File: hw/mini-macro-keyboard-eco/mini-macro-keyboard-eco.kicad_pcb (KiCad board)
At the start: 2 copper layers, 0 parts

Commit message: feat(hw): load netlist
Signed-off-by: Ivan Kovalenko <s1ckretbox@gmail.com>
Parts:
- added C0: 100n, Capacitor_SMD:C_0402_1005Metric, F.Cu at (64.6, 43.6)
- added C1: 100n, Capacitor_SMD:C_0402_1005Metric, F.Cu at (64.6, 45.6)
- added C10: 1u, Capacitor_SMD:C_0402_1005Metric, F.Cu at (79.3, 29.8)
- added C11: 1u, Capacitor_SMD:C_0402_1005Metric, F.Cu at (69.3, 41.1)
- added C2: 100n, Capacitor_SMD:C_0402_1005Metric, F.Cu at (82.2, 29.8)
- added C3: 100n, Capacitor_SMD:C_0402_1005Metric, F.Cu at (57.6, 53.7)
- added C4: 100n, Capacitor_SMD:C_0402_1005Metric, F.Cu at (63.5, 47.9)
- added C5: 100n, Capacitor_SMD:C_0402_1005Metric, F.Cu at (67.4, 43.0)
- added C6: 100n, Capacitor_SMD:C_0402_1005Metric, F.Cu at (79.3, 31.8)
- added C7: 4.7u, Capacitor_SMD:C_0402_1005Metric, F.Cu at (73.4, 38.5)
- added C8: 12p, Capacitor_SMD:C_0402_1005Metric, F.Cu at (60.6, 49.9)
- added C9: 12p, Capacitor_SMD:C_0402_1005Metric, F.Cu at (82.2, 27.8)
- added D1: BLUE, LED_SMD:LED_0603_1608Metric, F.Cu at (63.0, 38.8)
- added D2: BLUE, LED_SMD:LED_0603_1608Metric, F.Cu at (67.0, 38.8)
- added D3: BLUE, LED_SMD:LED_0603_1608Metric, F.Cu at (63.0, 41.4)
- added J0: USB_B_Micro, Connector_USB:USB_Micro-B_Molex-105017-0001, F.Cu at (46.2, 40.5)
- added J1: SWD, Connector_PinHeader_2.54mm:PinHeader_1x04_P2.54mm_Horizontal, F.Cu at (19.6, 39.8)
- added R0: 10k, Resistor_SMD:R_0402_1005Metric, F.Cu at (28.8, 50.7)
- added R1: 10k, Resistor_SMD:R_0402_1005Metric, F.Cu at (28.8, 52.7)
- added R11: 330, Resistor_SMD:R_0603_1608Metric, F.Cu at (61.1, 45.6)
- added R12: 330, Resistor_SMD:R_0603_1608Metric, F.Cu at (79.9, 25.6)
- added R13: 330, Resistor_SMD:R_0603_1608Metric, F.Cu at (79.9, 23.1)
- added R2: 10k, Resistor_SMD:R_0402_1005Metric, F.Cu at (60.6, 47.9)
- added R3: 10k, Resistor_SMD:R_0402_1005Metric, F.Cu at (51.8, 53.7)
- added R4: 10k, Resistor_SMD:R_0402_1005Metric, F.Cu at (66.4, 41.1)
- added R5: 10k, Resistor_SMD:R_0402_1005Metric, F.Cu at (79.3, 27.8)
- added R6: 10k, Resistor_SMD:R_0402_1005Metric, F.Cu at (70.5, 38.5)
- added R7: 47, Resistor_SMD:R_0402_1005Metric, F.Cu at (54.7, 53.7)
- added SW0: SW_SPDT, Button_Switch_SMD:SW_SPDT_PCM12, F.Cu at (45.5, 49.0)
- added SW1: SW_1, Button_Switch_Keyboard:SW_Cherry_MX_1.00u_PCB, F.Cu at (29.9, 22.3)
- added SW2: SW_2, Button_Switch_Keyboard:SW_Cherry_MX_1.00u_PCB, F.Cu at (50.1, 22.3)
- added SW3: SW_3, Button_Switch_Keyboard:SW_Cherry_MX_1.00u_PCB, F.Cu at (70.3, 22.3)
- added SW4: RESET, Button_Switch_THT:SW_PUSH_6mm, F.Cu at (32.7, 39.5)
- added SW5: SW_SPDT, Button_Switch_SMD:SW_SPDT_PCM12, F.Cu at (56.0, 40.5)
- added SW6: SW_SPDT, Button_Switch_SMD:SW_SPDT_PCM12, F.Cu at (35.6, 49.0)
- added U1: USBLC6-2SC6, Package_TO_SOT_SMD:SOT-23-6, F.Cu at (25.0, 52.1)
- added U2: XC6206P322MR, Package_TO_SOT_SMD:SOT-23, F.Cu at (80.1, 19.6)
- added U3: STM32F070F6Px, Package_SO:TSSOP-20_4.4x6.5mm_P0.65mm, F.Cu at (54.8, 48.7)
- added Y1: 16 MHz, Crystal:Crystal_SMD_3225-4Pin_3.2x2.5mm, F.Cu at (19.9, 52.0)

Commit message: feat(hw): add rough layout
Signed-off-by: Ivan Kovalenko <s1ckretbox@gmail.com>
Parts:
- moved J1 151.3 mm to (162.7, 89.0), turned to 90 degrees
- moved SW6 131.9 mm to (163.3, 81.9), turned to 180 degrees
- moved SW4 124.4 mm to (149.2, 83.1)
- moved R13 121.8 mm to (167.1, 108.2)
- moved R3 121.5 mm to (166.9, 92.8)
- moved U1 121.4 mm to (141.1, 87.2), turned to 90 degrees
- moved SW1 120.9 mm to (126.4, 95.2)
- moved SW2 120.4 mm to (145.9, 95.2)
- moved D3 120.3 mm to (163.0, 108.2), turned to 180 degrees
- moved SW3 119.9 mm to (165.5, 95.2)
- moved C3 118.0 mm to (168.9, 92.8)
- moved Y1 112.1 mm to (125.9, 88.2), turned to 180 degrees
- moved R12 107.2 mm to (148.1, 108.2)
- moved R1 106.6 mm to (127.6, 92.8)
- moved J0 105.4 mm to (142.9, 82.3), turned to 180 degrees
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
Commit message: fix(hw): remove debounce circuit from the mechanical switches
Signed-off-by: Ivan Kovalenko <s1ckretbox@gmail.com>
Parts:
- removed C1, C2, C3: 100n, Capacitor_SMD:C_0402_1005Metric
- removed R1, R2, R3: 10k, Resistor_SMD:R_0402_1005Metric
- J0: value USB_B_Micro -> USB
- J1: value SWD -> DEBUG_SWD
- SW0: value SW_SPDT -> BOOT
- SW1: value SW_1 -> SW_Cherry_MX_1.00u_PCB
- SW2: value SW_2 -> SW_Cherry_MX_1.00u_PCB
- SW3: value SW_3 -> SW_Cherry_MX_1.00u_PCB
- SW5: value SW_SPDT -> LAYOUT
- SW6: value SW_SPDT -> BACKLIGHT
- U3: value STM32F070F6Px -> STM32F070F6P6
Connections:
- U3 pad 8: Net-(U3-Pad8) -> (no net)

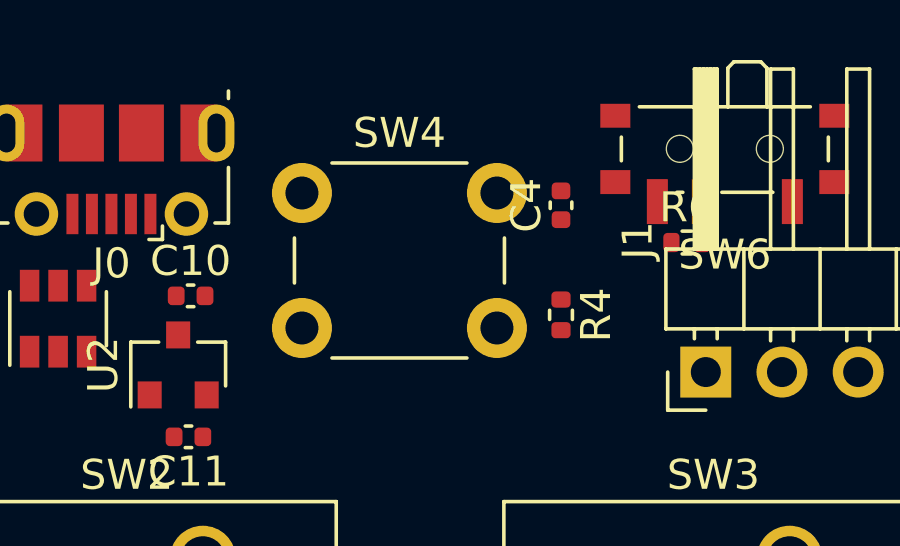
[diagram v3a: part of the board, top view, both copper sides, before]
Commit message: feat(hw)!: remove reset push button
BREAKING CHANGE:
I remove the reset schematic becauce it uses a lot of space and
I won't mess with usb bootloaders in the future. Also I don't know
how to update software on the MCU in the user-friendly manner.

Signed-off-by: Ivan Kovalenko <s1ckretbox@gmail.com>
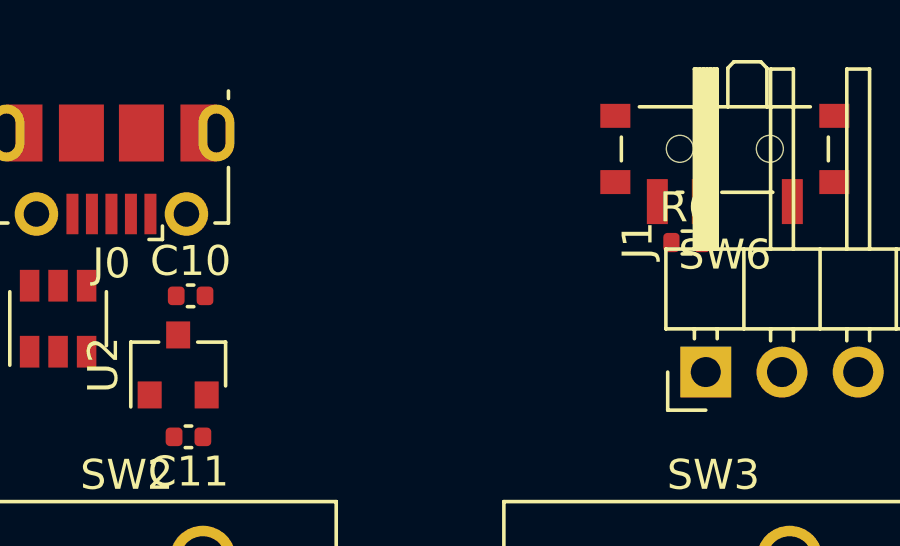
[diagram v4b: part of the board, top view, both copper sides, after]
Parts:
- removed C4: 100n, Capacitor_SMD:C_0402_1005Metric
- removed R4: 10k, Resistor_SMD:R_0402_1005Metric
- removed SW4: RESET, Button_Switch_THT:SW_PUSH_6mm
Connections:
- U3 pad 4: NRST -> (no net)

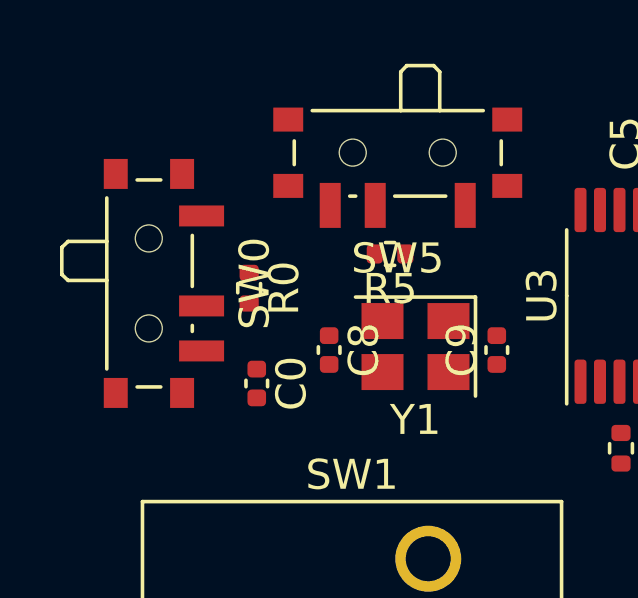
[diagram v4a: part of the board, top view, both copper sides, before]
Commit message: feat(hw)!: remove boot switch
I have removed boot switch because I don't expect to use another
bootloaders

Signed-off-by: Ivan Kovalenko <s1ckretbox@gmail.com>
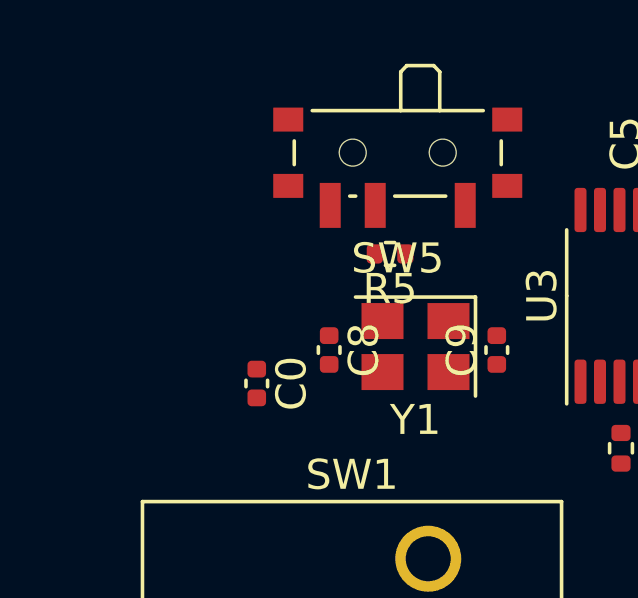
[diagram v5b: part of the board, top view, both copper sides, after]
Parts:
- removed R0: 10k, Resistor_SMD:R_0402_1005Metric
- removed SW0: BOOT, Button_Switch_SMD:SW_SPDT_PCM12
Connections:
- U3 pad 1: BOOT0 -> GND

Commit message: feat(hw): reanotate schematic
Signed-off-by: Ivan Kovalenko <s1ckretbox@gmail.com>
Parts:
- renumbered C9 to C0, C8 to C1, C5 to C2, C6 to C3, C7 to C4, C10 to C5, C11 to C6, C0 to C7, R7 to R0, R11 to R1, R12 to R2, R13 to R3

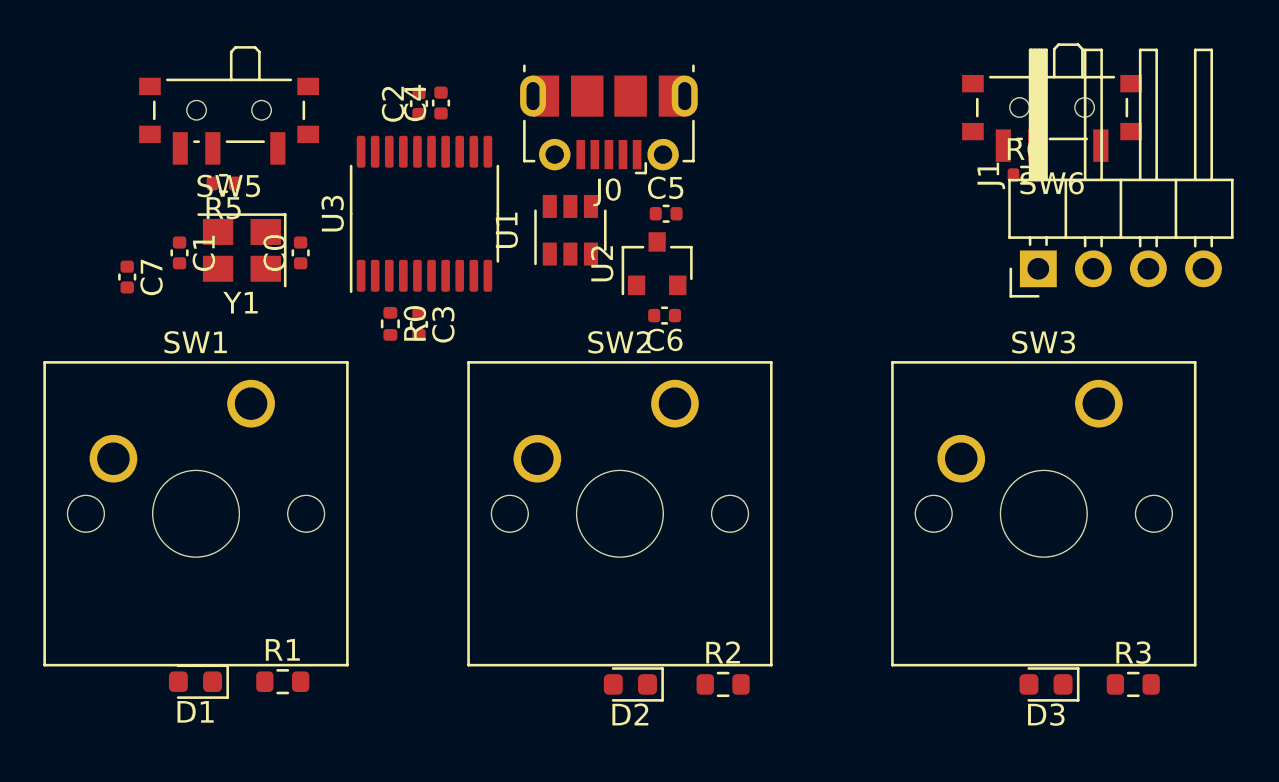
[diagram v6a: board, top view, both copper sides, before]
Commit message: feat(hw): place components closer
Signed-off-by: Ivan Kovalenko <s1ckretbox@gmail.com>
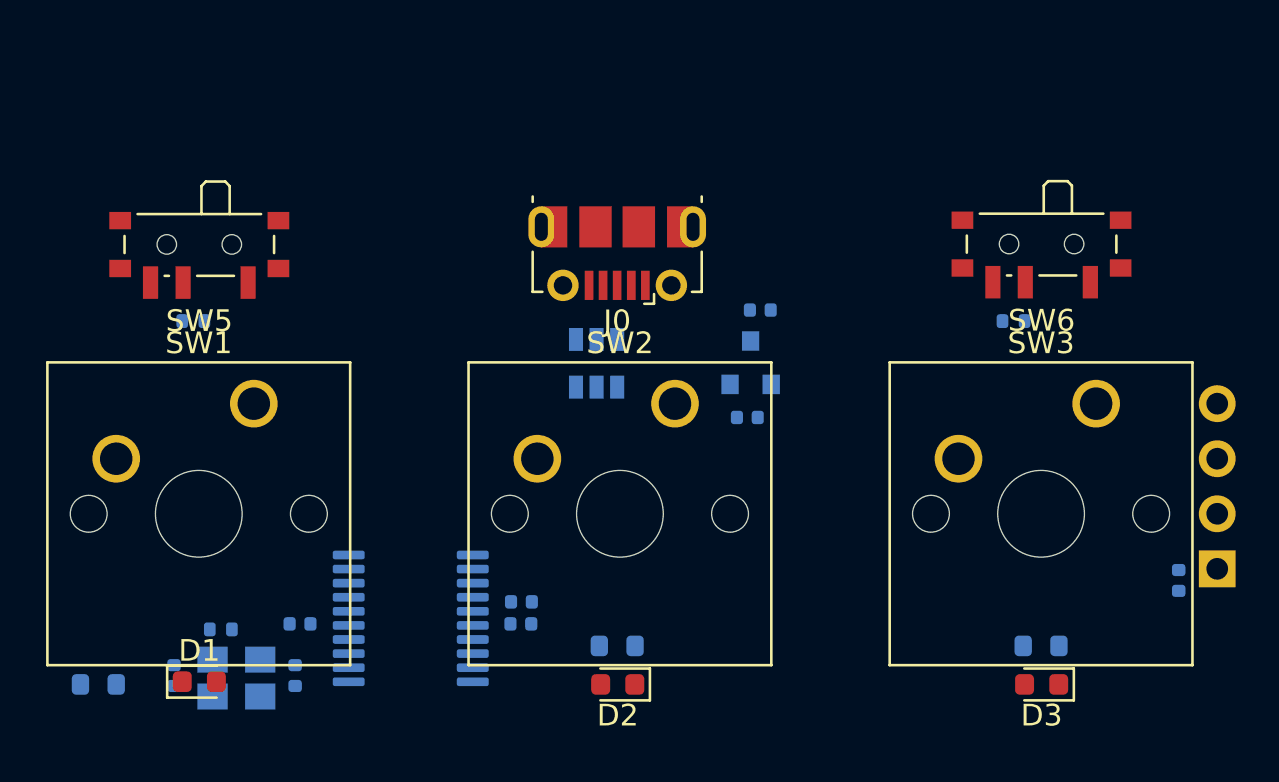
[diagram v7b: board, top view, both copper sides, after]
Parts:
- C0, C1, C2, C3, C4, C5, C6, C7, J1, R0, R1, R2, R3, R5, R6, U1, U2, U3, Y1: moved to B.Cu
- moved C7 50.5 mm to (169.2, 103.4)
- moved C2 24.5 mm to (138.8, 105.4), turned to 0 degrees
- moved C4 23.3 mm to (138.8, 104.4), turned to 0 degrees
- moved Y1 19.7 mm to (125.7, 107.9)
- moved C0 19.5 mm to (128.4, 107.8), turned to 270 degrees
- moved C1 19.5 mm to (122.8, 107.8), turned to 90 degrees
- moved U3 18.7 mm to (133.7, 105.2), turned to 0 degrees
- moved R0 16.1 mm to (125.0, 105.7), turned to 180 degrees
- moved J1 16.1 mm to (170.9, 102.9), turned to 0 degrees
- moved C3 14.9 mm to (128.6, 105.4), turned to 180 degrees
- moved R1 8.51 mm to (119.3, 108.2), turned to 180 degrees
- moved R6 6.75 mm to (161.5, 91.4)
- moved R5 6.50 mm to (123.7, 91.4)
- moved SW5 6.34 mm to (124.0, 88.2)
- moved SW6 6.32 mm to (162.8, 88.2)
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
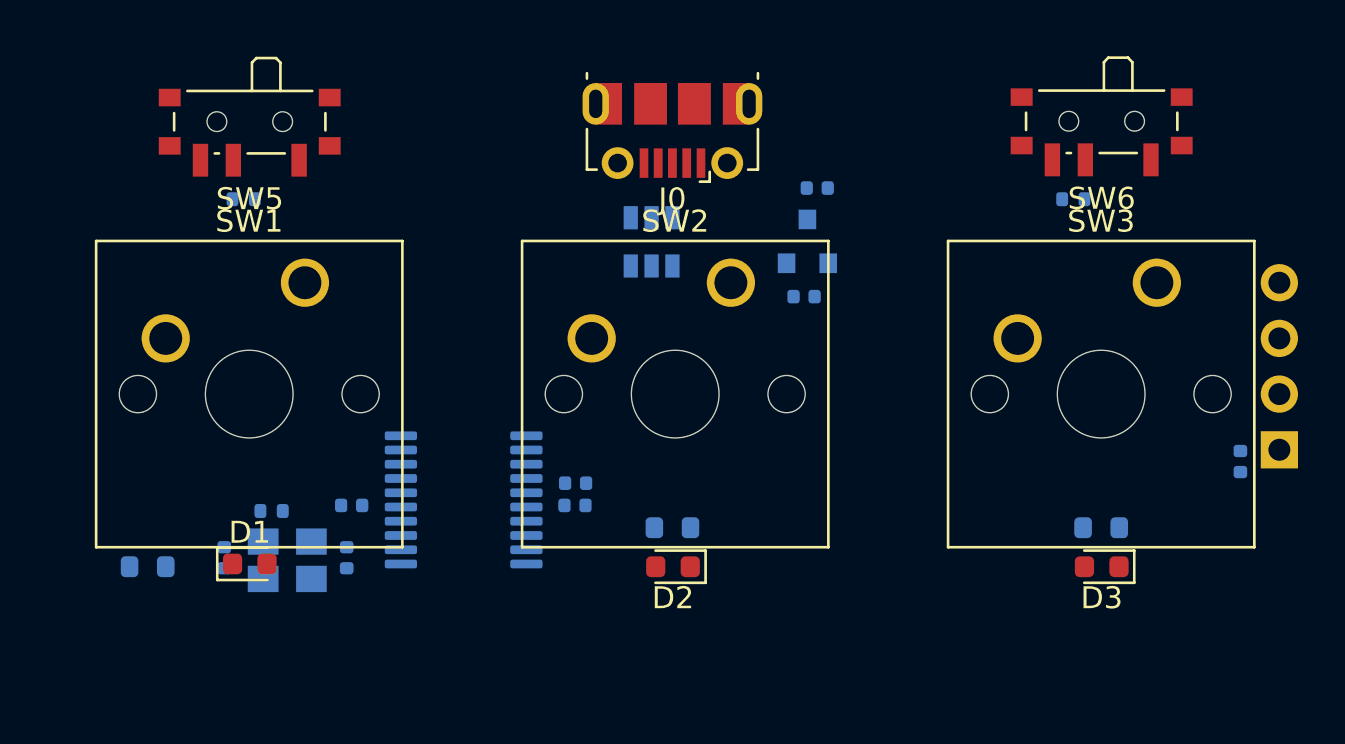
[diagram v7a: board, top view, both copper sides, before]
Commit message: feat(hw): add mounting holes
Signed-off-by: Ivan Kovalenko <s1ckretbox@gmail.com>
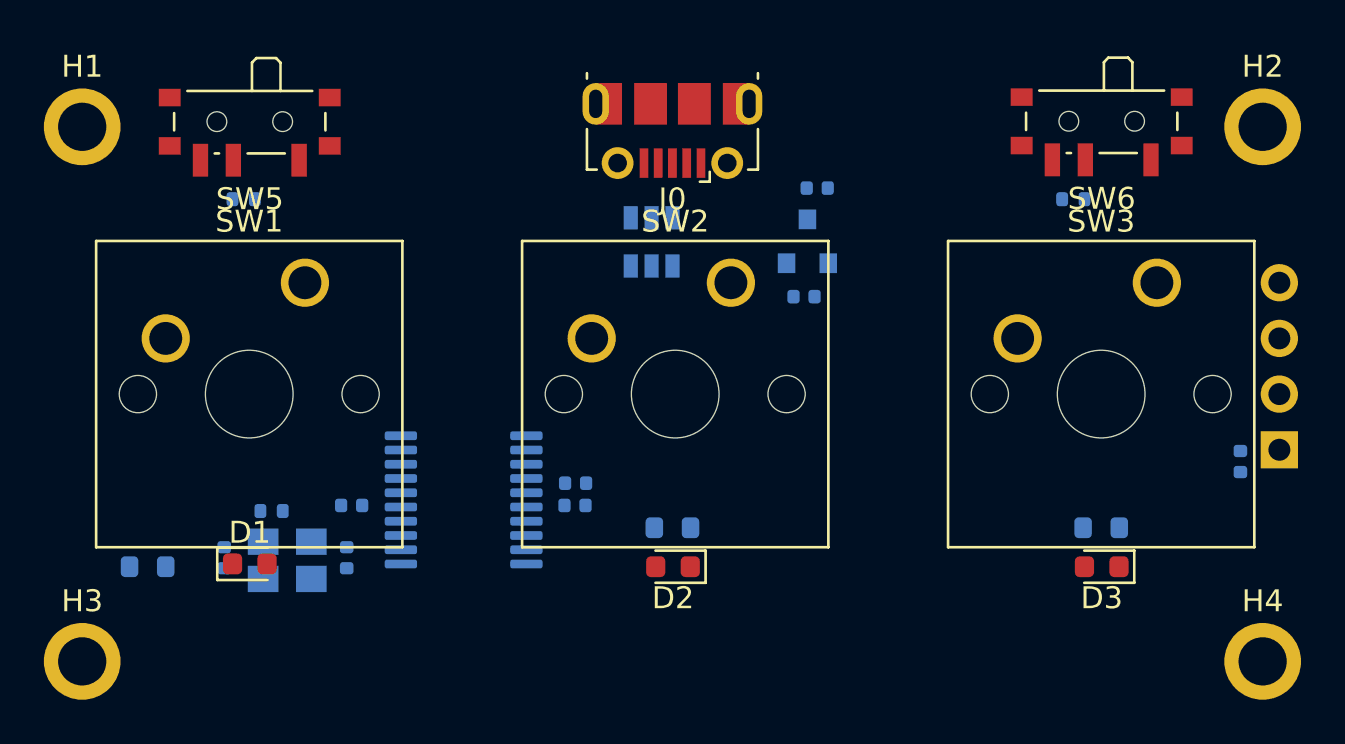
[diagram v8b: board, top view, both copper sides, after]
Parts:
- added H1: MountingHole_Pad, MountingHole:MountingHole_2.2mm_M2_ISO7380_Pad, F.Cu at (116.3, 88.1)
- added H2: MountingHole_Pad, MountingHole:MountingHole_2.2mm_M2_ISO7380_Pad, F.Cu at (170.2, 88.1)
- added H3: MountingHole_Pad, MountingHole:MountingHole_2.2mm_M2_ISO7380_Pad, F.Cu at (116.3, 112.5)
- added H4: MountingHole_Pad, MountingHole:MountingHole_2.2mm_M2_ISO7380_Pad, F.Cu at (170.2, 112.5)
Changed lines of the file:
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@@
     (tracks 0)
     (zones 0)
-    (modules 28)
+    (modules 32)
     (nets 27)
   )
@@
     (add_net USB_D-)
   )
+  (module MountingHole:MountingHole_2.2mm_M2_ISO7380_Pad (layer F.Cu)
+    (at 170.18 112.522)
+    (descr "Mounting Hole 2.2mm, M2, ISO7380")
+    (tags "mounting hole 2.2mm m2 iso7380")
+    (attr virtual)
+    (fp_text reference H4 (at 0 -2.75) (layer F.SilkS)
+      (effects (font (size 1 1) (thickness 0.15)))
+    )
+    (fp_text value MountingHole_Pad (at 0 2.75) (layer F.Fab)
+      (effects (font (size 1 1) (thickness 0.15)))
+    )
+    (fp_text user %R (at 0.3 0) (layer F.Fab)
+      (effects (font (size 1 1) (thickness 0.15)))
+    )
+    (fp_circle (center 0 0) (end 1.75 0) (layer Cmts.User) (width 0.15))
+    (fp_circle (center 0 0) (end 2 0) (layer F.CrtYd) (width 0.05))
+    (pad 1 thru_hole circle (at 0 0) (size 3.5 3.5) (drill 2.2) (layers *.Cu *.Mask)
+      (net 1 GND))
+  )
+  (module MountingHole:MountingHole_2.2mm_M2_ISO7380_Pad (layer F.Cu)
+    (at 116.332 112.522)
+    (descr "Mounting Hole 2.2mm, M2, ISO7380")
+    (tags "mounting hole 2.2mm m2 iso7380")
+    (attr virtual)
+    (fp_text reference H3 (at 0 -2.75) (layer F.SilkS)
+      (effects (font (size 1 1) (thickness 0.15)))
+    )
+    (fp_text value MountingHole_Pad (at 0 2.75) (layer F.Fab)
+      (effects (font (size 1 1) (thickness 0.15)))
+    )
+    (fp_text user %R (at 0.3 0) (layer F.Fab)
+      (effects (font (size 1 1) (thickness 0.15)))
+    )
+    (fp_circle (center 0 0) (end 1.75 0) (layer Cmts.User) (width 0.15))
+    (fp_circle (center 0 0) (end 2 0) (layer F.CrtYd) (width 0.05))
+    (pad 1 thru_hole circle (at 0 0) (size 3.5 3.5) (drill 2.2) (layers *.Cu *.Mask)
+      (net 1 GND))
+  )
+  (module MountingHole:MountingHole_2.2mm_M2_ISO7380_Pad (layer F.Cu)
+    (at 170.18 88.138)
+    (descr "Mounting Hole 2.2mm, M2, ISO7380")
+    (tags "mounting hole 2.2mm m2 iso7380")
+    (attr virtual)
+    (fp_text reference H2 (at 0 -2.75) (layer F.SilkS)
+      (effects (font (size 1 1) (thickness 0.15)))
+    )
+    (fp_text value MountingHole_Pad (at 0 2.75) (layer F.Fab)
+      (effects (font (size 1 1) (thickness 0.15)))
+    )
+    (fp_text user %R (at 0.3 0) (layer F.Fab)
+      (effects (font (size 1 1) (thickness 0.15)))
+    )
+    (fp_circle (center 0 0) (end 1.75 0) (layer Cmts.User) (width 0.15))
+    (fp_circle (center 0 0) (end 2 0) (layer F.CrtYd) (width 0.05))
+    (pad 1 thru_hole circle (at 0 0) (size 3.5 3.5) (drill 2.2) (layers *.Cu *.Mask)
+      (net 1 GND))
+  )
+  (module MountingHole:MountingHole_2.2mm_M2_ISO7380_Pad (layer F.Cu)
+    (at 116.332 88.138)
+    (descr "Mounting Hole 2.2mm, M2, ISO7380")
+    (tags "mounting hole 2.2mm m2 iso7380")
+    (attr virtual)
+    (fp_text reference H1 (at 0 -2.75) (layer F.SilkS)
+      (effects (font (size 1 1) (thickness 0.15)))
+    )
+    (fp_text value MountingHole_Pad (at 0 2.75) (layer F.Fab)
+      (effects (font (size 1 1) (thickness 0.15)))
+    )
+    (fp_text user %R (at 0.3 0) (layer F.Fab)
+      (effects (font (size 1 1) (thickness 0.15)))
+    )
+    (fp_circle (center 0 0) (end 1.75 0) (layer Cmts.User) (width 0.15))
+    (fp_circle (center 0 0) (end 2 0) (layer F.CrtYd) (width 0.05))
+    (pad 1 thru_hole circle (at 0 0) (size 3.5 3.5) (drill 2.2) (layers *.Cu *.Mask)
+      (net 1 GND))
+  )
   (module Capacitor_SMD:C_0402_1005Metric (layer B.Cu)
